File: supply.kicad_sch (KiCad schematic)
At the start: 156 parts, among them J7 BarrelJack_Pin2mm_MJ-179PH, J8 JST_SH_1x4_BM04B-SRSS-TB-LF-SN, Q12 SI7613DN-T1-GE3, Q13 SI7613DN-T1-GE3, Q14 BSS138PW, Q15 BSS138PW, Q16 BSS138PW, Q17 BSS138PW, SW4 SW_CVS-08TB, SW5 SW_KMR211NGLFS_SMD, U17 LTC4412IS6, U18 LTC4412IS6, U19 MPM54304GMN, U20 MPM54304GMN, U21 NCP718BSN330T1G, U22 MAX16150A_SOT, U25 PAC1954T-E_VQFN, U26 MAX812REUS+T, U27 MP8869S, U28 XC6230H001ER-G, U29 MCP4726A0T_DFN, U30 PAC1954T-E_VQFN, U31 LM3880

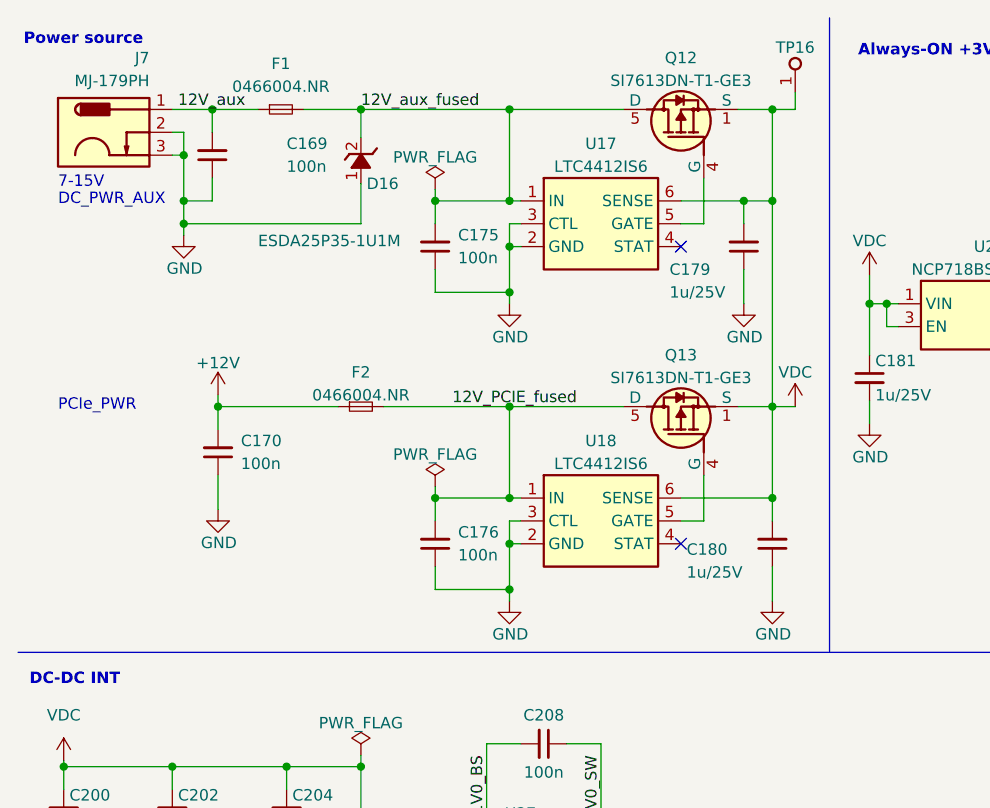
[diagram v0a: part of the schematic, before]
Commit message: Removing PCIe from sch and PCB
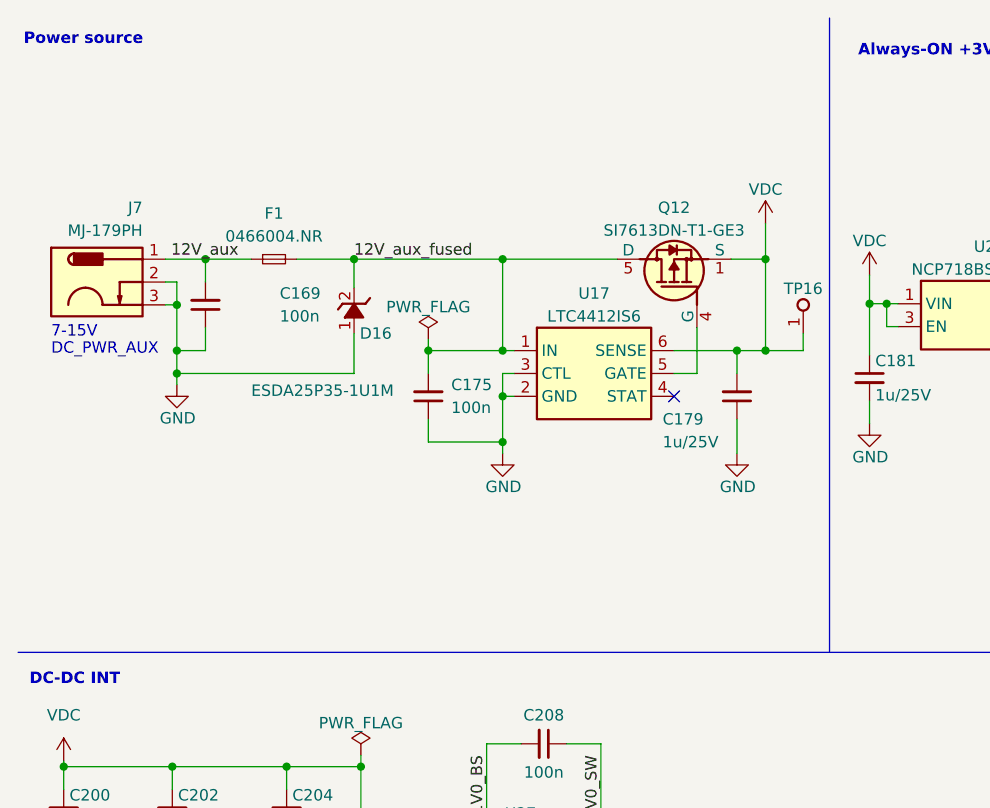
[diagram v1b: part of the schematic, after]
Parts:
- removed C170, C176: C_100n_0402, antmicro-footprints:C_0402_1005Metric, symbol antmicroCapacitors0402:C_100n_0402
- removed C180: C_1u_25V_0603, antmicro-footprints:C_0603_1608Metric, symbol antmicroCapacitors0603:C_1u_25V_0603
- removed F2: F_4A_1206, antmicro-footprints:F_1206_3216Metric, symbol antmicroFuses:F_4A_1206
- removed Q13: SI7613DN-T1-GE3, antmicro-footprints:Vishay_PowerPAK_1212-8_Single, symbol antmicroTransistorsFETsMOSFETsSingle:SI7613DN-T1-GE3
- removed U18: LTC4412IS6, antmicro-footprints:SOT-23-6, symbol antmicroPMICORControllersIdealDiodes:LTC4412IS6
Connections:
- no-connect marks 7 -> 6
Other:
- note removed: "PCIe_PWR"
- moved on the sheet: C169, C175, C179, D16, F1, J7, Q12, TP16, U17
